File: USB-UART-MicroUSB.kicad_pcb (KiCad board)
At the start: 2 copper layers, 33 x 24.5 mm, 25 parts, among them J1 USB_B_Micro, J2 Conn_01x09_Male, Q1 MMBT2222A, Q2 MMBT2222A, U1 CP2102N-A01-GQFN24, U2 AP1117-33

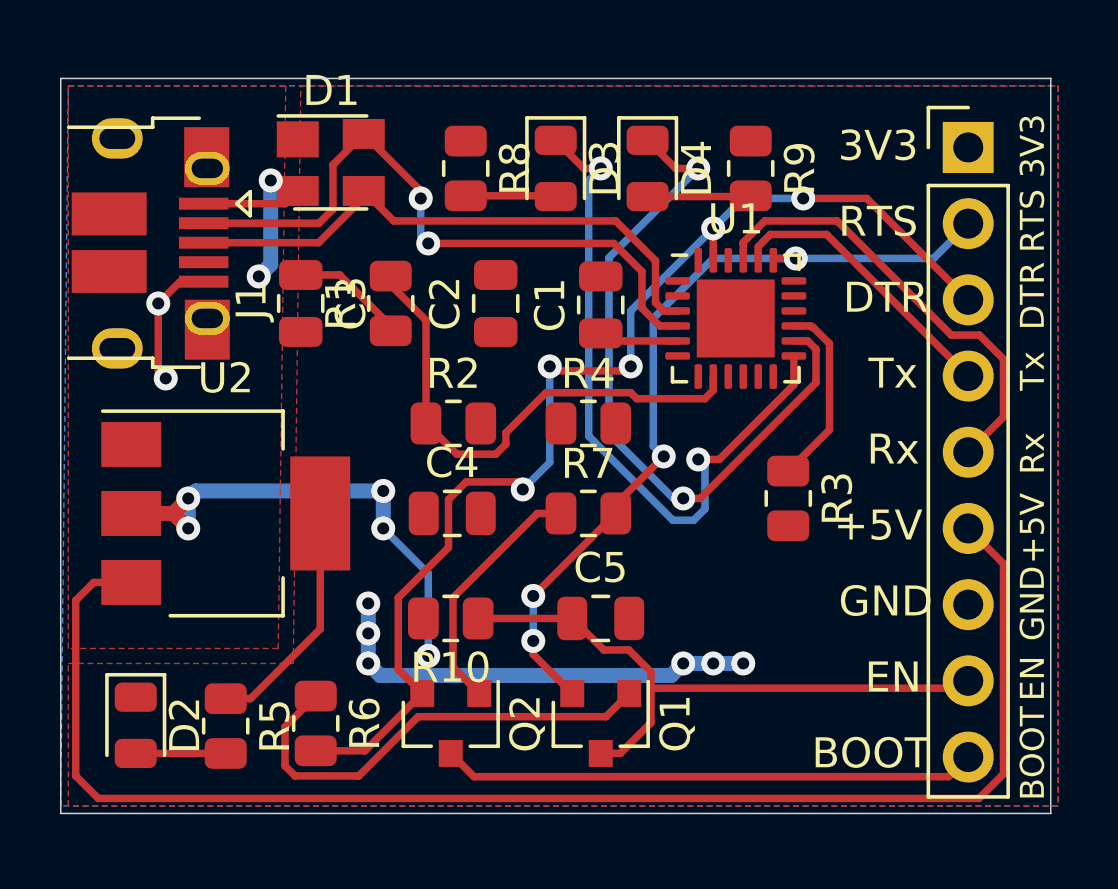
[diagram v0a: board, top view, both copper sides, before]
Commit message: Changed CP2102N to QFN28 (for availability reasons). Layout done.
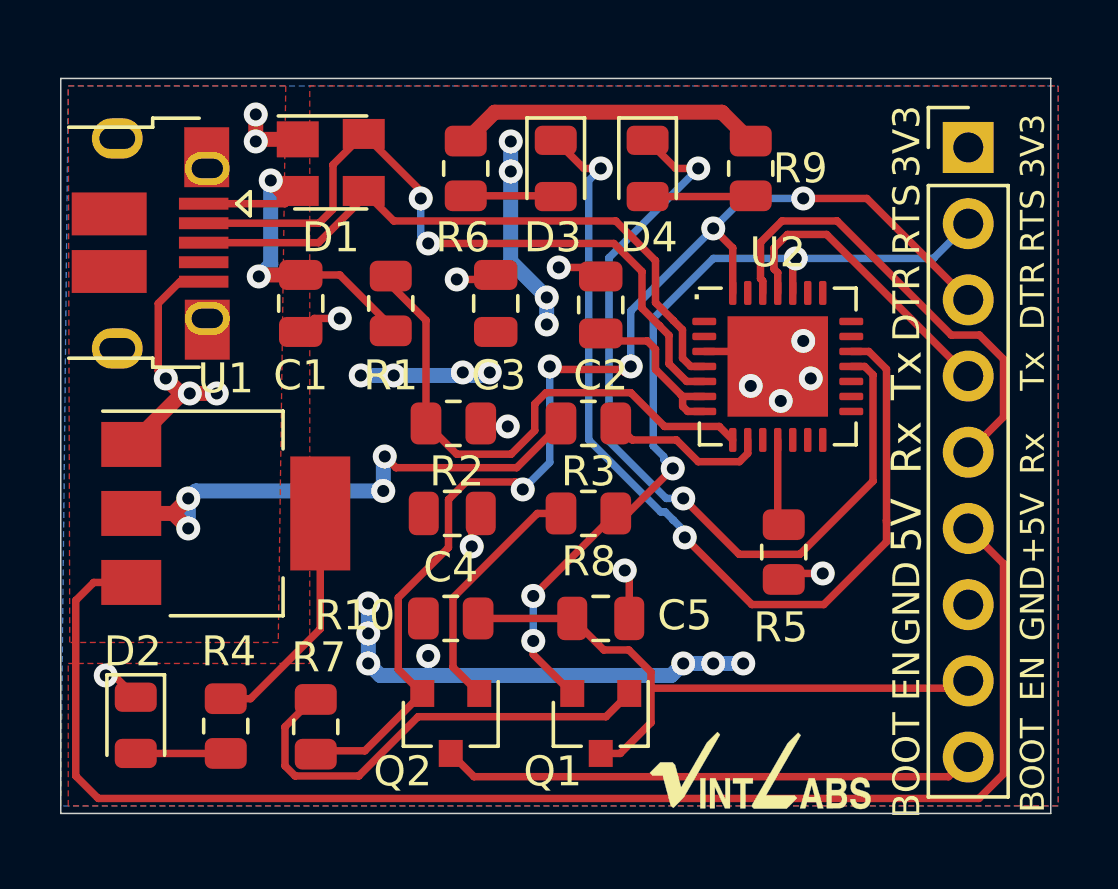
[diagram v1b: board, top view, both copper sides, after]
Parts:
- removed the U1 at (165.5, 52.5)
- added G***: LOGO, USB-UART-MicroUSB:logo-name-3mm, B.Cu at (147.0, 67.4)
- added G***: LOGO, USB-UART-MicroUSB:logo-name-3mm, F.Cu at (166.4, 67.6)
- added U2: CP2102N-A01-GQFN28, Package_DFN_QFN:QFN-28-1EP_5x5mm_P0.5mm_EP3.35x3.35mm, F.Cu at (166.9, 54.1)
- C5: value 0.1u -> 4.7u
- moved R5 1.79 mm to (167.1, 60.3)
- moved R7 0.11 mm to (151.5, 66.1)
- renumbered C3 to C1, C1 to C2, C2 to C3, R4 to R3, R5 to R4, R3 to R5, R8 to R6, R6 to R7, R7 to R8, U2 to U1
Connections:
- J2 pad 4: TxD -> RxD
- J2 pad 5: RxD -> TxD
- U1 pad 1: Net-(U2-Pad1) -> GND
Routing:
- net VDD: track 42.2 -> 68.8 mm, vias 11 -> 19
- net GND: track 4.42 -> 25.2 mm, vias 2 -> 17
- net RXT: track 23.1 -> 31.6 mm
- net TxD: track 9.58 -> 15.6 mm
- net Net-(R3-Pad2): track 0.00 -> 5.49 mm
- net TXT: track 23.5 -> 28.5 mm
- net RxD: track 15.1 -> 10.2 mm
- net Net-(R5-Pad1): track 6.25 -> 2.91 mm
- net VBus: track 58.7 -> 61.2 mm
- net USB_DP: track 19.1 -> 21.3 mm
- net USB_DN: track 22.1 -> 24.4 mm
- net DTR: track 39.2 -> 40.8 mm
- net RTS: track 27.6 -> 28.8 mm
- net Net-(R1-Pad2): track 17.1 -> 18.1 mm
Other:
- board text added: "."
- board text added: "3.3V CP2102N USB UART"
- board text added: "5V"
- board text added: "Usage info at: http://github.com/ vintlabs/USB-UART-MicroUSB"
- board text added: "Use EN and BOOT for programming ESP boards"
- board text added: "http://vintlabs.com"
